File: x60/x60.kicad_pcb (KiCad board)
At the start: 2 copper layers, 140 parts, among them SW1 SW_Push, U1 ATmega32U4-AU, Y1 16mhz

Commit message: arranged the keys on the pcb
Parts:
- added MX65: CAPS Stepped, MX_Only:MXOnly-1.5U-NoLED, F.Cu at (242.1, 125.4)
- MX1, MX23, MX5, MX61: footprint MX_Alps_Hybrid:MX-1U-NoLED -> MX_Only:MXOnly-1.5U-NoLED
- MX10, MX11, MX12, MX13, MX14, MX15, MX16, MX17, MX18, MX19, MX2, MX20, MX21, MX22, MX24, MX25, MX26, MX27, MX28, MX29, MX30, MX31, MX32, MX33, MX34, MX35, MX37, MX38, MX39, MX40, MX41, MX42, MX43, MX44, MX45, MX46, MX47, MX48, MX50, MX51, MX52, MX55, MX56, MX6, MX62, MX7, MX8, MX9: footprint MX_Alps_Hybrid:MX-1U-NoLED -> MX_Only:MXOnly-1U-NoLED
- MX3, MX58: footprint MX_Alps_Hybrid:MX-1U-NoLED -> MX_Only:MXOnly-1.75U-NoLED
- MX36: footprint MX_Alps_Hybrid:MX-1U-NoLED -> MX_Only:MXOnly-7U-NoLED
- MX4, MX57: footprint MX_Alps_Hybrid:MX-1U-NoLED -> MX_Only:MXOnly-2.25U-NoLED
- MX49: value ALT -> RALT; footprint MX_Alps_Hybrid:MX-1U-NoLED -> MX_Only:MXOnly-1.5U-NoLED
- MX53: footprint MX_Alps_Hybrid:MX-1U-NoLED -> MX_Only:MXOnly-2.75U-NoLED
- MX54: value WIN -> RWIN; footprint MX_Alps_Hybrid:MX-1U-NoLED -> MX_Only:MXOnly-1U-NoLED
- MX59: value CTRL -> RCTRL; footprint MX_Alps_Hybrid:MX-1U-NoLED -> MX_Only:MXOnly-1.5U-NoLED
- MX60: footprint MX_Alps_Hybrid:MX-1U-NoLED -> MX_Only:MXOnly-2U-NoLED
- MX63: value \ -> \ Split; footprint MX_Alps_Hybrid:MX-1U-NoLED -> MX_Only:MXOnly-1U-NoLED
- MX64: value ` -> ` Split; footprint MX_Alps_Hybrid:MX-1U-NoLED -> MX_Only:MXOnly-1U-NoLED
- moved MX62 239.7 mm to (273.8, 18.3)
- moved MX59 236.5 mm to (269.1, 37.3)
- moved MX53 220.5 mm to (257.2, 18.3)
- moved MX61 218.7 mm to (269.1, -19.8)
- moved MX8 218.5 mm to (40.5, -0.79)
- moved MX58 218.1 mm to (247.7, 18.3)
- moved MX57 212.1 mm to (261.9, -0.79)
- moved MX46 193.5 mm to (197.6, -38.9)
- moved MX6 190.4 mm to (35.7, -19.8)
- moved MX13 189.9 mm to (69.1, 18.3)
- moved MX5 187.1 mm to (11.9, 37.3)
- moved MX12 182.4 mm to (59.5, -0.79)
- moved MX56 176.3 mm to (245.3, -19.8)
- moved MX54 173.9 mm to (245.3, 37.3)
- moved MX15 172.3 mm to (73.8, -19.8)
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
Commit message: added stepped caps
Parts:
- MX65: footprint MX_Only:MXOnly-1.5U-NoLED -> MX_Only:MXOnly-1.25U-NoLED
- moved MX65 243.0 mm to (11.9, 47.6)
- moved MX1 48.5 mm to (14.3, 28.6)
- moved MX10 48.5 mm to (57.1, 28.6)
- moved MX12 48.5 mm to (61.9, 47.6)
- moved MX15 48.5 mm to (76.2, 28.6)
- moved MX17 48.5 mm to (81.0, 47.6)
- moved MX20 48.5 mm to (95.2, 28.6)
- moved MX21 48.5 mm to (100.0, 47.6)
- moved MX24 48.5 mm to (114.3, 28.6)
- moved MX25 48.5 mm to (119.1, 47.6)
- moved MX29 48.5 mm to (133.3, 28.6)
- moved MX3 48.5 mm to (16.7, 47.6)
- moved MX30 48.5 mm to (138.1, 47.6)
- moved MX33 48.5 mm to (152.4, 28.6)
- moved MX34 48.5 mm to (157.2, 47.6)
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
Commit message: wired and arranged 1.25u bottom row
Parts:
- added D63: D_Small, Diode_SMD:D_SOD-123, F.Cu at (127.0, -31.0)
- added MX66: LCTRL1.25, MX_Only:MXOnly-1.25U-NoLED, F.Cu at (11.9, 85.7)
- added MX67: LWIN1.25, MX_Only:MXOnly-1.25U-NoLED, F.Cu at (35.7, 85.7)
- added MX68: LALT1.25, MX_Only:MXOnly-1.25U-NoLED, F.Cu at (59.5, 85.7)
- added MX69: SPACE6.25, MX_Only:MXOnly-6.25U-NoLED, F.Cu at (131.0, 85.7)
- added MX70: RALT1.25, MX_Only:MXOnly-1.25U-NoLED, F.Cu at (202.4, 85.7)
- added MX71: RWIN1.25, MX_Only:MXOnly-1.25U-NoLED, F.Cu at (226.2, 85.7)
- added MX72: Menu1.25, MX_Only:MXOnly-1.25U-NoLED, F.Cu at (250.0, 85.7)
- added MX73: RCTRL1.25, MX_Only:MXOnly-1.25U-NoLED, F.Cu at (273.8, 85.7)
- moved C1 57.9 mm to (130.3, 176.1)
- moved C2 57.9 mm to (140.5, 172.7)
- moved C4 57.9 mm to (136.1, 170.2)
- moved C6 57.9 mm to (141.8, 166.8)
- moved D1 57.9 mm to (125.3, 173.7)
- moved D11 57.9 mm to (131.0, 163.7)
- moved D12 57.9 mm to (90.8, 173.7)
- moved D13 57.9 mm to (96.5, 173.7)
- moved D14 57.9 mm to (113.8, 163.7)
- moved D15 57.9 mm to (102.3, 173.7)
- moved D18 57.9 mm to (119.5, 163.7)
- moved D19 57.9 mm to (125.3, 163.7)
- moved D26 57.9 mm to (142.5, 163.7)
- moved D27 57.9 mm to (108.0, 173.7)
- moved D31 57.9 mm to (85.0, 173.7)
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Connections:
- MX59 pad 1: COL13 -> COL14
- MX59 pad 2: Net-(D58-Pad2) -> Net-(D63-Pad2)

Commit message: adjusted diodes top row
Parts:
- moved D59 260.6 mm to (250.0, 9.53), turned to 90 degrees
- moved D54 242.2 mm to (246.1, 9.53), turned to 90 degrees
- moved D50 231.5 mm to (227.0, 9.53), turned to 90 degrees
- moved D46 201.1 mm to (217.5, 29.4), turned to 90 degrees
- moved D1 196.4 mm to (17.5, 9.53), turned to 90 degrees
- moved D45 193.6 mm to (208.0, 9.53), turned to 90 degrees
- moved D37 193.3 mm to (169.9, 9.53), turned to 90 degrees
- moved D41 179.7 mm to (188.9, 9.59), turned to 90 degrees
- moved D6 171.6 mm to (36.5, 9.59), turned to 90 degrees
- moved D32 168.5 mm to (150.8, 9.53), turned to 90 degrees
- moved D15 166.5 mm to (74.6, 9.53), turned to 90 degrees
- moved D10 161.3 mm to (55.6, 9.53), turned to 90 degrees
- moved D24 160.8 mm to (112.7, 9.53), turned to 90 degrees
- moved D33 159.8 mm to (160.3, 29.4), turned to 90 degrees
- moved D28 157.6 mm to (131.8, 9.53), turned to 90 degrees
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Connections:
- MX19 pad 1: Net-(MX19-Pad1) -> COL5

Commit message: aligned diodes
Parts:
- moved D61 282.9 mm to (284.2, 9.53), turned to 90 degrees
- moved D55 261.0 mm to (246.1, 8.73), turned to 90 degrees
- moved D51 245.1 mm to (236.5, 29.4), turned to 90 degrees
- moved D56 235.1 mm to (255.6, 29.4), turned to 90 degrees
- moved D58 234.6 mm to (258.8, 84.9), turned to 90 degrees
- moved D57 228.1 mm to (247.7, 47.6), turned to 90 degrees
- moved D60 227.2 mm to (281.8, 29.4), turned to 90 degrees
- moved D47 226.3 mm to (222.2, 47.6), turned to 90 degrees
- moved D62 199.9 mm to (284.2, 66.7), turned to 90 degrees
- moved D63 194.6 mm to (283.4, 84.9), turned to 90 degrees
- moved D48 190.2 mm to (229.4, 66.7), turned to 90 degrees
- moved D42 182.1 mm to (198.4, 29.4), turned to 90 degrees
- moved D52 180.9 mm to (241.3, 47.6), turned to 90 degrees
- moved D2 179.1 mm to (26.2, 29.4), turned to 90 degrees
- moved D43 168.0 mm to (203.2, 47.6), turned to 90 degrees
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
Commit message: fixed diode arrangement
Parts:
- D1, D10, D11, D12, D13, D14, D15, D16, D17, D18, D19, D2, D20, D21, D22, D23, D24, D25, D26, D27, D28, D29, D3, D30, D31, D32, D33, D34, D35, D36, D37, D38, D39, D4, D40, D41, D42, D43, D44, D45, D46, D47, D48, D49, D5, D50, D51, D52, D53, D54, D55, D56, D57, D58, D59, D6, D60, D61, D62, D63, D7, D8, D9, MX40: moved to B.Cu
- moved D48 3.97 mm to (233.4, 66.7), turned to 270 degrees
- moved D55 0.79 mm to (246.1, 9.53), turned to 270 degrees
- turned D1 to 270 degrees
- turned D10 to 270 degrees
- turned D11 to 270 degrees
- turned D12 to 270 degrees
- turned D13 to 270 degrees
- turned D14 to 270 degrees
- turned D15 to 270 degrees
- turned D16 to 270 degrees
- turned D17 to 270 degrees
- turned D18 to 270 degrees
- turned D19 to 270 degrees
- turned D2 to 270 degrees
- turned D20 to 270 degrees
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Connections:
- MX20 pad 1: Net-(MX20-Pad1) -> COL5
- MX21 pad 1: Net-(MX21-Pad1) -> COL5
- MX22 pad 1: Net-(MX22-Pad1) -> COL5
- MX23 pad 1: Net-(MX23-Pad1) -> COL5

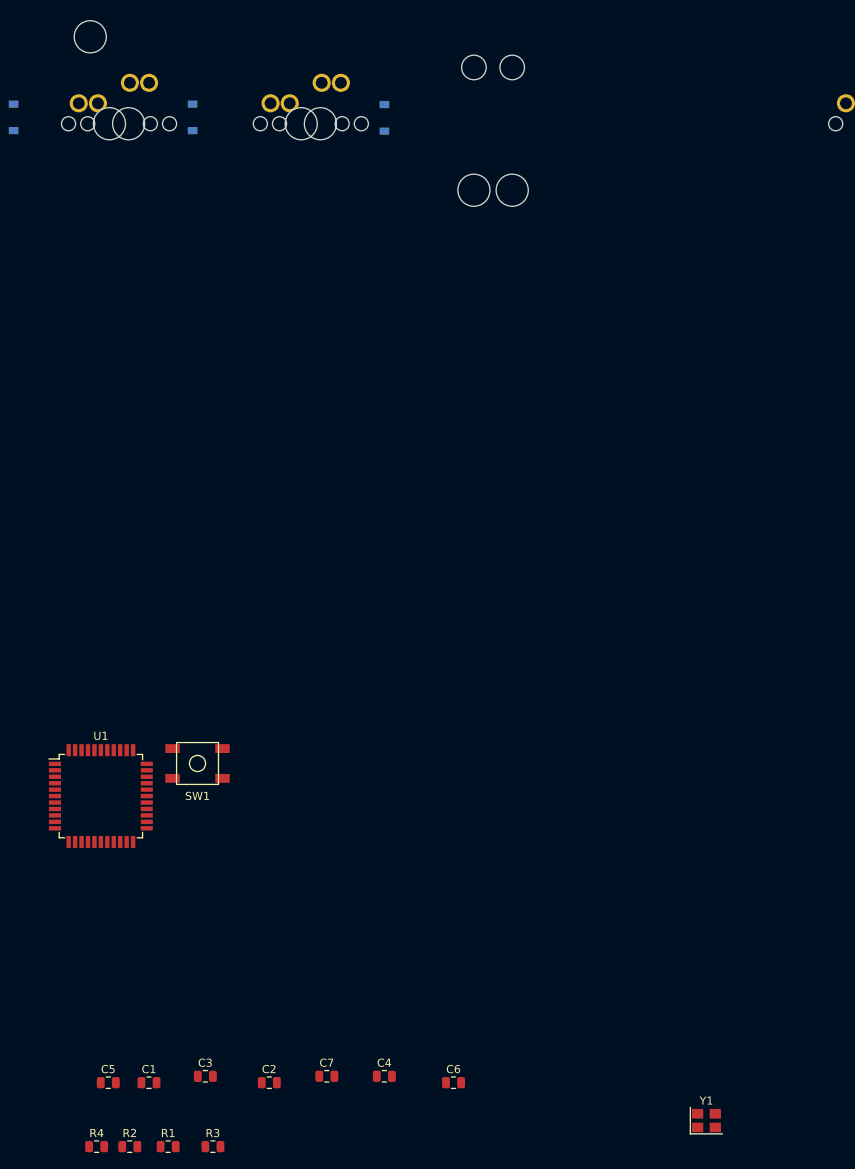
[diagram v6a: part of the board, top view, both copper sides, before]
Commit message: placed mcu
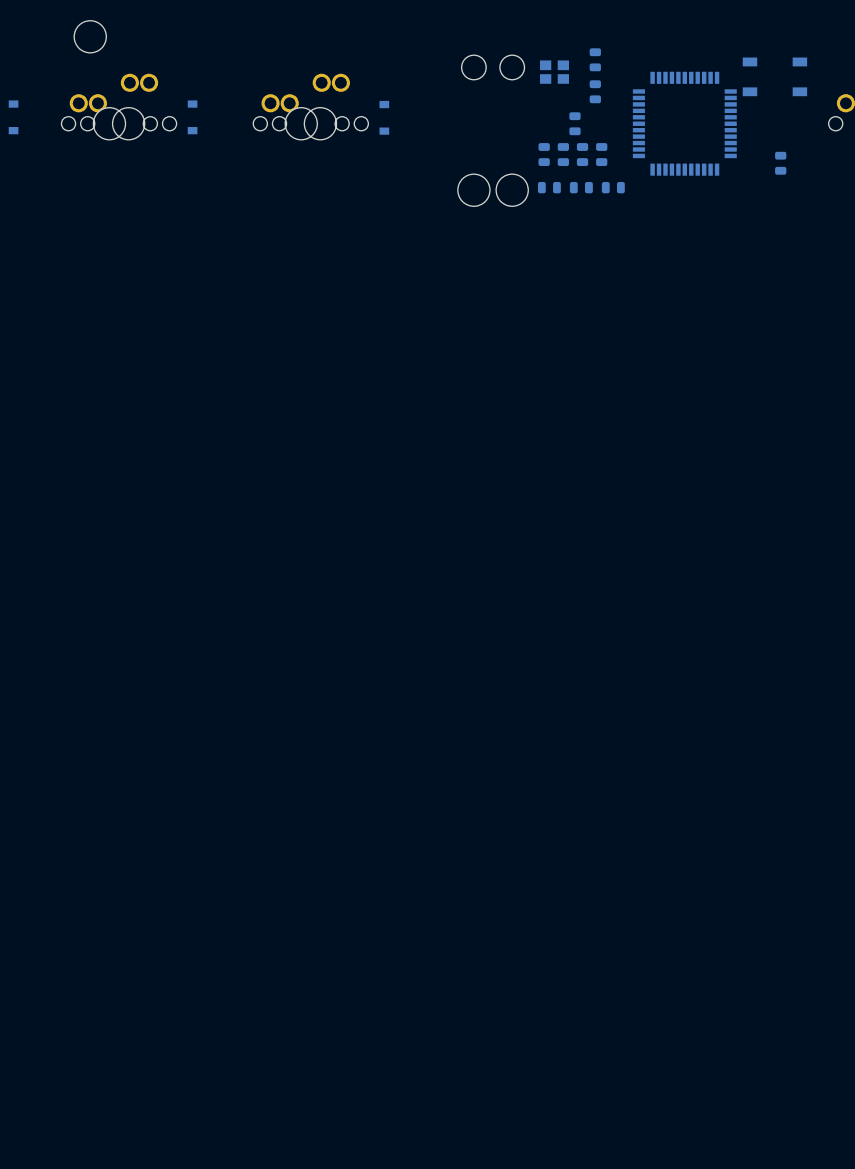
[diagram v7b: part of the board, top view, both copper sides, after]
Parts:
- C1, C2, C3, C4, C5, C6, C7, R1, R2, R3, R4, SW1, U1, Y1: moved to B.Cu
- moved R4 148.7 mm to (119.1, 90.6), turned to 90 degrees
- moved C3 135.2 mm to (96.0, 77.8), turned to 270 degrees
- moved C5 132.4 mm to (93.5, 85.7), turned to 270 degrees
- moved Y1 131.5 mm to (91.0, 79.3), turned to 180 degrees
- moved R2 130.0 mm to (90.3, 93.7), turned to 180 degrees
- moved R1 129.6 mm to (94.3, 93.7)
- moved C2 129.5 mm to (96.0, 81.8), turned to 270 degrees
- moved R3 129.0 mm to (98.3, 93.7)
- moved C1 128.2 mm to (96.8, 89.5), turned to 90 degrees
- moved C7 117.6 mm to (89.7, 89.5), turned to 90 degrees
- moved C4 117.1 mm to (94.5, 89.5), turned to 90 degrees
- moved C6 116.0 mm to (92.1, 89.5), turned to 90 degrees
- moved SW1 111.4 mm to (118.3, 79.9)
- moved U1 110.6 mm to (107.2, 85.7)

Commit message: fixed routing of mcu
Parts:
- moved D57 30.2 mm to (277.8, 47.6), turned to 90 degrees
- moved C6 28.4 mm to (119.1, 80.8)
- moved SW1 26.6 mm to (92.1, 84.1), turned to 270 degrees
- moved C4 21.5 mm to (115.9, 91.3), turned to 180 degrees
- moved Y1 19.5 mm to (110.0, 75.1)
- moved C2 18.7 mm to (113.5, 75.1), turned to 90 degrees
- moved R3 18.4 mm to (97.6, 75.3), turned to 270 degrees
- moved C1 14.4 mm to (100.0, 75.5)
- moved R2 12.1 mm to (98.8, 85.0), turned to 90 degrees
- moved C7 12.0 mm to (101.6, 91.3), turned to 180 degrees
- moved C3 9.45 mm to (105.1, 75.0)
- moved R1 6.83 mm to (98.7, 88.4), turned to 270 degrees
- moved C5 6.63 mm to (98.8, 81.6)
- moved U1 2.24 mm to (109.0, 84.5)
- moved R4 1.97 mm to (120.5, 89.3)
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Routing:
- net GND: track 0.00 -> 101.8 mm
- net +5V: track 0.00 -> 65.3 mm, vias 0 -> 4
- net Net-(R3-Pad2): track 0.00 -> 19.4 mm
- net Net-(C3-Pad1): track 0.00 -> 10.1 mm
- net Net-(C5-Pad1): track 0.00 -> 7.53 mm
- net Net-(C2-Pad1): track 0.00 -> 6.31 mm
- net Net-(R4-Pad2): track 0.00 -> 5.84 mm
- net Net-(R1-Pad1): track 0.00 -> 4.86 mm
- net Net-(R2-Pad1): track 0.00 -> 4.63 mm
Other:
- net class Default: trace_width 0.25 -> 0.254
- net class power added: clearance 0.2, trace_width 0.381, via_dia 0.8, via_drill 0.4
- board text added: "x60"
